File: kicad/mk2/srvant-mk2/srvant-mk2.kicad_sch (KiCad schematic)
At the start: 0 parts

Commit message: work on schematics
* add power rail
* import CM4 related part
* design most of the BMC-PHY part
* create new library/footprint for rp t113-s3 SOM
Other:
- added sheet bmc (bmc.kicad_sch)
- added sheet cm4 (cm4_main.kicad_sch)
- added sheet interconnection (interconnection.kicad_sch)
- added sheet power (power.kicad_sch)
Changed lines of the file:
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@@
     (rev "0.1")
+  )
+  (sheet (at 262.89 95.25) (size 68.58 96.52) (fields_autoplaced)
+    (stroke (width 0.1524) (type solid))
+    (fill (color 0 0 0 0.0000))
+    (property "Sheetname" "cm4" (at 262.89 94.5384 0)
+      (effects (font (size 1.27 1.27)) (justify left bottom))
+    )
+    (property "Sheetfile" "cm4_main.kicad_sch" (at 262.89 192.3546 0)
+      (effects (font (size 1.27 1.27)) (justify left top))
+    )
+    (instances
+      (project "srvant-mk2"
+        (path "/1859a578-b791-4142-bdf4-fda494df1146" (page "5"))
+      )
+    )
+  )
+  (sheet (at 54.61 111.76) (size 55.88 55.88) (fields_autoplaced)
+    (stroke (width 0.1524) (type solid))
+    (fill (color 0 0 0 0.0000))
+    (property "Sheetname" "bmc" (at 54.61 111.0484 0)
+      (effects (font (size 1.27 1.27)) (justify left bottom))
+    )
+    (property "Sheetfile" "bmc.kicad_sch" (at 54.61 168.2246 0)
+      (effects (font (size 1.27 1.27)) (justify left top))
+    )
+    (instances
+      (project "srvant-mk2"
+        (path "/1859a578-b791-4142-bdf4-fda494df1146" (page "3"))
+      )
+    )
+  )
+  (sheet (at 147.32 107.95) (size 57.15 76.2) (fields_autoplaced)
+    (stroke (width 0.1524) (type solid))
+    (fill (color 0 0 0 0.0000))
+    (property "Sheetname" "interconnection" (at 147.32 107.2384 0)
+      (effects (font (size 1.27 1.27)) (justify left bottom))
+    )
+    (property "Sheetfile" "interconnection.kicad_sch" (at 147.32 184.7346 0)
+      (effects (font (size 1.27 1.27)) (justify left top))
+    )
+    (instances
+      (project "srvant-mk2"
+        (path "/1859a578-b791-4142-bdf4-fda494df1146" (page "4"))
+      )
+    )
+  )
+  (sheet (at 41.91 25.4) (size 69.85 38.1) (fields_autoplaced)
+    (stroke (width 0.1524) (type solid))
+    (fill (color 0 0 0 0.0000))
+    (property "Sheetname" "power" (at 41.91 24.6884 0)
+      (effects (font (size 1.27 1.27)) (justify left bottom))
+    )
+    (property "Sheetfile" "power.kicad_sch" (at 41.91 64.0846 0)
+      (effects (font (size 1.27 1.27)) (justify left top))
+    )
+    (pin "+BATT" output (at 111.76 39.37 0)
+      (effects (font (size 1.27 1.27)) (justify right))
+    )
+    (pin "+5v" output (at 111.76 41.91 0)
+      (effects (font (size 1.27 1.27)) (justify right))
+    )
+    (instances
+      (project "srvant-mk2"
+        (path "/1859a578-b791-4142-bdf4-fda494df1146" (page "2"))
+      )
+    )
   )
   (sheet_instances

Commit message: more progress
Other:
- sheet bmc ports: added +5v; removed none
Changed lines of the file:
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@@
     (rev "0.1")
+  )
+  (wire (pts (xy 105.41 85.09) (xy 132.08 85.09))
+    (stroke (width 0) (type default))
+  )
+  (wire (pts (xy 132.08 41.91) (xy 111.76 41.91))
+    (stroke (width 0) (type default))
+  )
+  (wire (pts (xy 132.08 85.09) (xy 132.08 41.91))
+    (stroke (width 0) (type default))
+  )
+  (wire (pts (xy 105.41 111.76) (xy 105.41 85.09))
+    (stroke (width 0) (type default))
   )
   (sheet (at 262.89 95.25) (size 68.58 96.52) (fields_autoplaced)
@@
       (effects (font (size 1.27 1.27)) (justify left top))
     )
+    (pin "+5v" input (at 105.41 111.76 90)
+      (effects (font (size 1.27 1.27)) (justify right))
+    )
     (instances

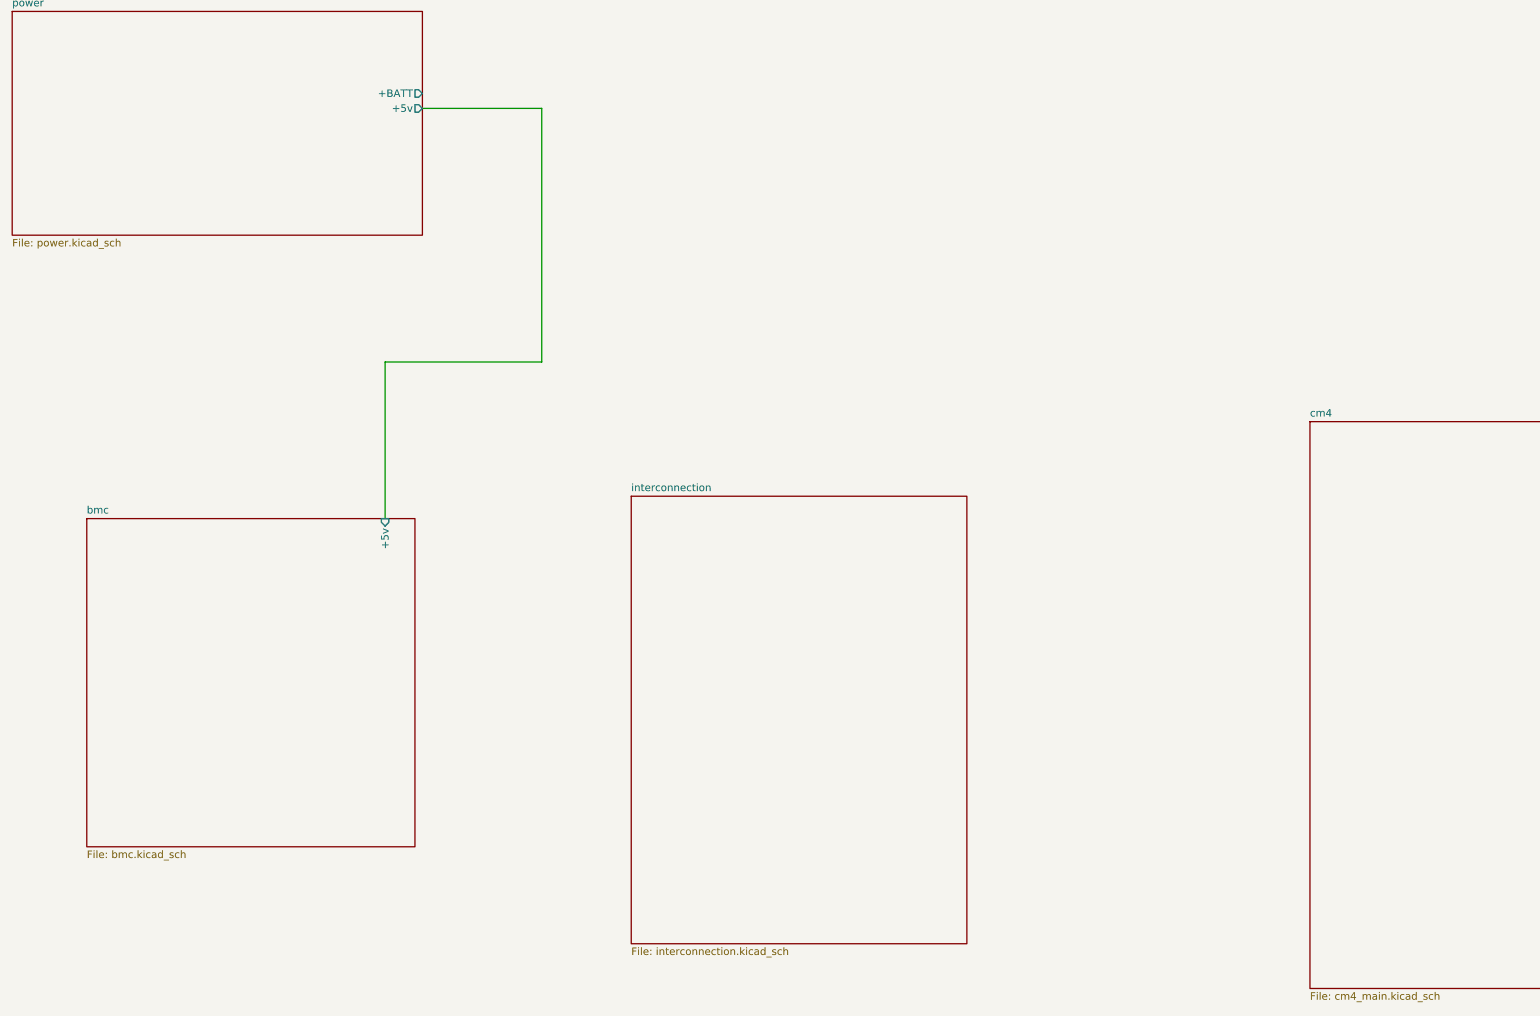
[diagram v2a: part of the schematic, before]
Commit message: merge cm4 into one page, basic interconnection
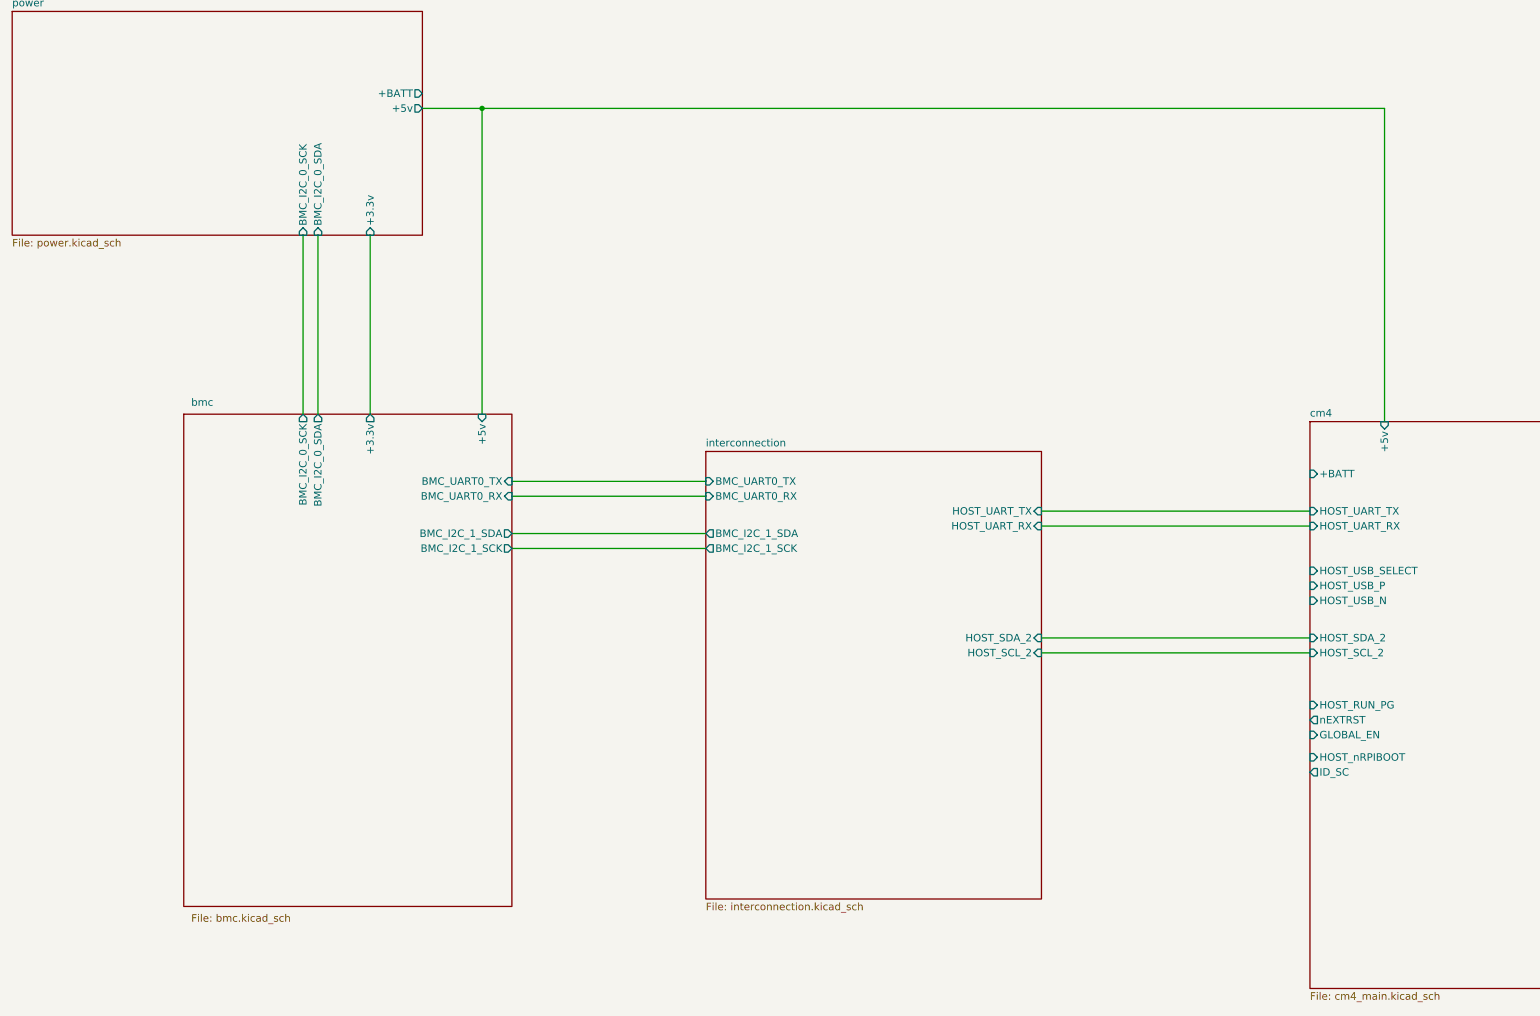
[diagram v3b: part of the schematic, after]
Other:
- sheet bmc ports: added +3.3v, BMC_I2C_0_SCK, BMC_I2C_0_SDA, BMC_I2C_1_SCK, BMC_I2C_1_SDA, BMC_UART0_RX, BMC_UART0_TX; removed none
- sheet cm4 ports: added +5v, +BATT, GLOBAL_EN, HOST_RUN_PG, HOST_SCL_2, HOST_SDA_2, HOST_UART_RX, HOST_UART_TX, HOST_USB_N, HOST_USB_P, HOST_USB_SELECT, HOST_nRPIBOOT, ID_SC, nEXTRST; removed none
- sheet interconnection ports: added BMC_I2C_1_SCK, BMC_I2C_1_SDA, BMC_UART0_RX, BMC_UART0_TX, HOST_SCL_2, HOST_SDA_2, HOST_UART_RX, HOST_UART_TX; removed none
- sheet power ports: added +3.3v, BMC_I2C_0_SCK, BMC_I2C_0_SDA; removed none
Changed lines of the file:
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@@
     (rev "0.1")
   )
-  (wire (pts (xy 105.41 85.09) (xy 132.08 85.09))
-    (stroke (width 0) (type default))
-  )
-  (wire (pts (xy 132.08 41.91) (xy 111.76 41.91))
-    (stroke (width 0) (type default))
-  )
-  (wire (pts (xy 132.08 85.09) (xy 132.08 41.91))
-    (stroke (width 0) (type default))
-  )
-  (wire (pts (xy 105.41 111.76) (xy 105.41 85.09))
-    (stroke (width 0) (type default))
+  (junction (at 121.92 41.91) (diameter 0) (color 0 0 0 0)
+  )
+  (wire (pts (xy 127 105.41) (xy 160.02 105.41))
+    (stroke (width 0) (type default))
+  )
+  (wire (pts (xy 93.98 63.5) (xy 93.98 93.98))
+    (stroke (width 0) (type default))
+  )
+  (wire (pts (xy 91.44 63.5) (xy 91.44 93.98))
+    (stroke (width 0) (type default))
+  )
+  (wire (pts (xy 217.17 134.62) (xy 262.89 134.62))
+    (stroke (width 0) (type default))
+  )
+  (wire (pts (xy 217.17 132.08) (xy 262.89 132.08))
+    (stroke (width 0) (type default))
+  )
+  (wire (pts (xy 217.17 110.49) (xy 262.89 110.49))
+    (stroke (width 0) (type default))
+  )
+  (wire (pts (xy 102.87 63.5) (xy 102.87 93.98))
+    (stroke (width 0) (type default))
+  )
+  (wire (pts (xy 127 107.95) (xy 160.02 107.95))
+    (stroke (width 0) (type default))
+  )
+  (wire (pts (xy 127 114.3) (xy 160.02 114.3))
+    (stroke (width 0) (type default))
+  )
+  (wire (pts (xy 111.76 41.91) (xy 121.92 41.91))
+    (stroke (width 1) (type default) (color 255 0 0 1))
+  )
+  (wire (pts (xy 127 116.84) (xy 160.02 116.84))
+    (stroke (width 0) (type default))
+  )
+  (wire (pts (xy 217.17 113.03) (xy 262.89 113.03))
+    (stroke (width 0) (type default))
+  )
+  (wire (pts (xy 121.92 41.91) (xy 121.92 93.98))
+    (stroke (width 1) (type default) (color 255 0 0 1))
+  )
+  (wire (pts (xy 121.92 41.91) (xy 275.59 41.91))
+    (stroke (width 1) (type default) (color 255 0 0 1))
+  )
+  (wire (pts (xy 275.59 95.25) (xy 275.59 41.91))
+    (stroke (width 1) (type default) (color 255 0 0 1))
   )
   (sheet (at 262.89 95.25) (size 68.58 96.52) (fields_autoplaced)
@@
     (property "Sheetfile" "cm4_main.kicad_sch" (at 262.89 192.3546 0)
       (effects (font (size 1.27 1.27)) (justify left top))
+    )
+    (pin "+BATT" input (at 262.89 104.14 180)
+      (effects (font (size 1.27 1.27)) (justify left))
+    )
+    (pin "+5v" input (at 275.59 95.25 90)
+      (effects (font (size 1.27 1.27)) (justify right))
+    )
+    (pin "nEXTRST" output (at 262.89 146.05 180)
+      (effects (font (size 1.27 1.27)) (justify left))
+    )
+    (pin "HOST_RUN_PG" input (at 262.89 143.51 180)
+      (effects (font (size 1.27 1.27)) (justify left))
+    )
+    (pin "GLOBAL_EN" input (at 262.89 148.59 180)
+      (effects (font (size 1.27 1.27)) (justify left))
+    )
+    (pin "HOST_nRPIBOOT" input (at 262.89 152.4 180)
+      (effects (font (size 1.27 1.27)) (justify left))
+    )
+    (pin "ID_SC" output (at 262.89 154.94 180)
+      (effects (font (size 1.27 1.27)) (justify left))
+    )
+    (pin "HOST_UART_TX" input (at 262.89 110.49 180)
+      (effects (font (size 1.27 1.27)) (justify left))
+    )
+    (pin "HOST_UART_RX" input (at 262.89 113.03 180)
+      (effects (font (size 1.27 1.27)) (justify left))
+    )
+    (pin "HOST_USB_SELECT" input (at 262.89 120.65 180)
+      (effects (font (size 1.27 1.27)) (justify left))
+    )
+    (pin "HOST_USB_P" input (at 262.89 123.19 180)
+      (effects (font (size 1.27 1.27)) (justify left))
+    )
+    (pin "HOST_USB_N" input (at 262.89 125.73 180)
+      (effects (font (size 1.27 1.27)) (justify left))
+    )
+    (pin "HOST_SCL_2" input (at 262.89 134.62 180)
+      (effects (font (size 1.27 1.27)) (justify left))
+    )
+    (pin "HOST_SDA_2" input (at 262.89 132.08 180)
+      (effects (font (size 1.27 1.27)) (justify left))
     )
     (instances
@@
     )
   )
-  (sheet (at 54.61 111.76) (size 55.88 55.88) (fields_autoplaced)
-    (stroke (width 0.1524) (type solid))
-    (fill (color 0 0 0 0.0000))
-    (property "Sheetname" "bmc" (at 54.61 111.0484 0)
-      (effects (font (size 1.27 1.27)) (justify left bottom))
-    )
-    (property "Sheetfile" "bmc.kicad_sch" (at 54.61 168.2246 0)
-      (effects (font (size 1.27 1.27)) (justify left top))
-    )
-    (pin "+5v" input (at 105.41 111.76 90)
+  (sheet (at 71.12 93.98) (size 55.88 83.82)
+    (stroke (width 0.1524) (type solid))
+    (fill (color 0 0 0 0.0000))
+    (property "Sheetname" "bmc" (at 72.39 92.71 0)
+      (effects (font (size 1.27 1.27)) (justify left bottom))
+    )
+    (property "Sheetfile" "bmc.kicad_sch" (at 72.39 179.07 0)
+      (effects (font (size 1.27 1.27)) (justify left top))
+    )
+    (pin "+5v" input (at 121.92 93.98 90)
+      (effects (font (size 1.27 1.27)) (justify right))
+    )
+    (pin "BMC_I2C_0_SDA" output (at 93.98 93.98 90)
+      (effects (font (size 1.27 1.27)) (justify right))
+    )
+    (pin "BMC_I2C_0_SCK" output (at 91.44 93.98 90)
+      (effects (font (size 1.27 1.27)) (justify right))
+    )
+    (pin "BMC_I2C_1_SCK" output (at 127 116.84 0)
+      (effects (font (size 1.27 1.27)) (justify right))
+    )
+    (pin "BMC_I2C_1_SDA" output (at 127 114.3 0)
+      (effects (font (size 1.27 1.27)) (justify right))
+    )
+    (pin "BMC_UART0_RX" input (at 127 107.95 0)
+      (effects (font (size 1.27 1.27)) (justify right))
+    )
+    (pin "BMC_UART0_TX" input (at 127 105.41 0)
+      (effects (font (size 1.27 1.27)) (justify right))
+    )
+    (pin "+3.3v" output (at 102.87 93.98 90)
       (effects (font (size 1.27 1.27)) (justify right))
     )
@@
     )
   )
-  (sheet (at 147.32 107.95) (size 57.15 76.2) (fields_autoplaced)
-    (stroke (width 0.1524) (type solid))
-    (fill (color 0 0 0 0.0000))
-    (property "Sheetname" "interconnection" (at 147.32 107.2384 0)
-      (effects (font (size 1.27 1.27)) (justify left bottom))
-    )
-    (property "Sheetfile" "interconnection.kicad_sch" (at 147.32 184.7346 0)
-      (effects (font (size 1.27 1.27)) (justify left top))
+  (sheet (at 160.02 100.33) (size 57.15 76.2) (fields_autoplaced)
+    (stroke (width 0.1524) (type solid))
+    (fill (color 0 0 0 0.0000))
+    (property "Sheetname" "interconnection" (at 160.02 99.6184 0)
+      (effects (font (size 1.27 1.27)) (justify left bottom))
+    )
+    (property "Sheetfile" "interconnection.kicad_sch" (at 160.02 177.1146 0)
+      (effects (font (size 1.27 1.27)) (justify left top))
+    )
+    (pin "BMC_UART0_RX" input (at 160.02 107.95 180)
+      (effects (font (size 1.27 1.27)) (justify left))
+    )
+    (pin "BMC_UART0_TX" input (at 160.02 105.41 180)
+      (effects (font (size 1.27 1.27)) (justify left))
+    )
+    (pin "HOST_UART_TX" input (at 217.17 110.49 0)
+      (effects (font (size 1.27 1.27)) (justify right))
+    )
+    (pin "HOST_UART_RX" input (at 217.17 113.03 0)
+      (effects (font (size 1.27 1.27)) (justify right))
+    )
+    (pin "BMC_I2C_1_SDA" output (at 160.02 114.3 180)
+      (effects (font (size 1.27 1.27)) (justify left))
+    )
+    (pin "BMC_I2C_1_SCK" output (at 160.02 116.84 180)
+      (effects (font (size 1.27 1.27)) (justify left))
+    )
+    (pin "HOST_SDA_2" input (at 217.17 132.08 0)
+      (effects (font (size 1.27 1.27)) (justify right))
+    )
+    (pin "HOST_SCL_2" input (at 217.17 134.62 0)
+      (effects (font (size 1.27 1.27)) (justify right))
     )
     (instances
@@
       (effects (font (size 1.27 1.27)) (justify right))
     )
-    (instances
+    (pin "BMC_I2C_0_SDA" input (at 93.98 63.5 270)
+      (effects (font (size 1.27 1.27)) (justify left))
+    )
+    (pin "+3.3v" input (at 102.87 63.5 270)
+      (effects (font (size 1.27 1.27)) (justify left))
+    )
+    (pin "BMC_I2C_0_SCK" input (at 91.44 63.5 270)
+      (effects (font (size 1.27 1.27)) (justify left))
+    )
+    (instances

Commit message: more progress
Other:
- sheet bmc ports: added +3.3v_BMC, +5v_BMC, +BATT, BMC_HOST_BT_nDis, BMC_HOST_EEPROM_nWP, BMC_HOST_POST_COMPLETE, BMC_HOST_POWER_EN, BMC_HOST_POWER_OUT, BMC_HOST_RESET_OUT, BMC_HOST_USB_DEMUX_CONTROL, BMC_HOST_WL_nDis, BMC_HOST_nRPIBOOT, BMC_SPI1_CLK, BMC_SPI1_CS, BMC_SPI1_MISO, BMC_SPI1_MOSI, BMC_USB_HOST_N, BMC_USB_HOST_P; removed +3.3v, +5v
- sheet cm4 ports: added +5v_HOST, HOST_BT_nDis, HOST_EEPROM_nWP, HOST_I2C_SLAVE_SCL, HOST_I2C_SLAVE_SDA, HOST_WL_nDis, USB_DEMUX_SELECT; removed +5v, HOST_SCL_2, HOST_SDA_2, HOST_USB_SELECT, ID_SC
- sheet interconnection ports: added BMC_HOST_BT_nDis, BMC_HOST_EEPROM_nWP, BMC_HOST_POST_COMPLETE, BMC_HOST_POWER_OUT, BMC_HOST_RESET_OUT, BMC_HOST_USB_DEMUX_CONTROL, BMC_HOST_WL_nDis, BMC_HOST_nRPIBOOT, BMC_USB_HOST_N, BMC_USB_HOST_P, HOST_BT_nDis, HOST_EEPROM_nWP, HOST_USB_N, HOST_USB_P, HOST_WL_nDis, USB_DEMUX_SELECT; removed none
- sheet power ports: added +3.3v_BMC, +5v_BMC, +5v_HOST, BMC_HOST_POWER_EN; removed +3.3v, +5v

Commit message: save state
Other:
- removed sheet interconnection
- added sheet BMC ethernet (bmc_eth.kicad_sch)
- sheet bmc ports: added BMC_UART1_RX, BMC_UART1_TX; removed BMC_SPI1_CLK, BMC_SPI1_CS, BMC_SPI1_MISO, BMC_SPI1_MOSI
- sheet cm4 ports: added +3.3v_HOST_PCIe, +5v_HOST_HDMI, HOST_GLOBAL_EN, HOST_UART4_RX, HOST_UART4_TX; removed GLOBAL_EN, nEXTRST
- sheet power ports: added +3.3v_HOST_PCIe, +5v_HOST_HDMI; removed none
- note added: "WL_nDisable: Drive low to disable Wireless (monitor on/off) BT_nDisable: Drive low to disable BT (monitor on/off) Global_EN: Pulling this pin low puts the CM4 in the lowest possible power-down state. After software shutdown, Global_EN needs to be pulled low for > 1ms to restart the power system on the CM4. RUN_PG: This pin when high signals that the CM4 has started. Driving this pin low resets th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"
- note added: "add additional UART connection for yet unknown purposes"
